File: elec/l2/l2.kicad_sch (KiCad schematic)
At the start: 26 parts, among them J1 Conn_01x06, J2 Conn_01x06, J3 Conn_01x04, U2 DEV-15583, U28 xiao-esp32c3

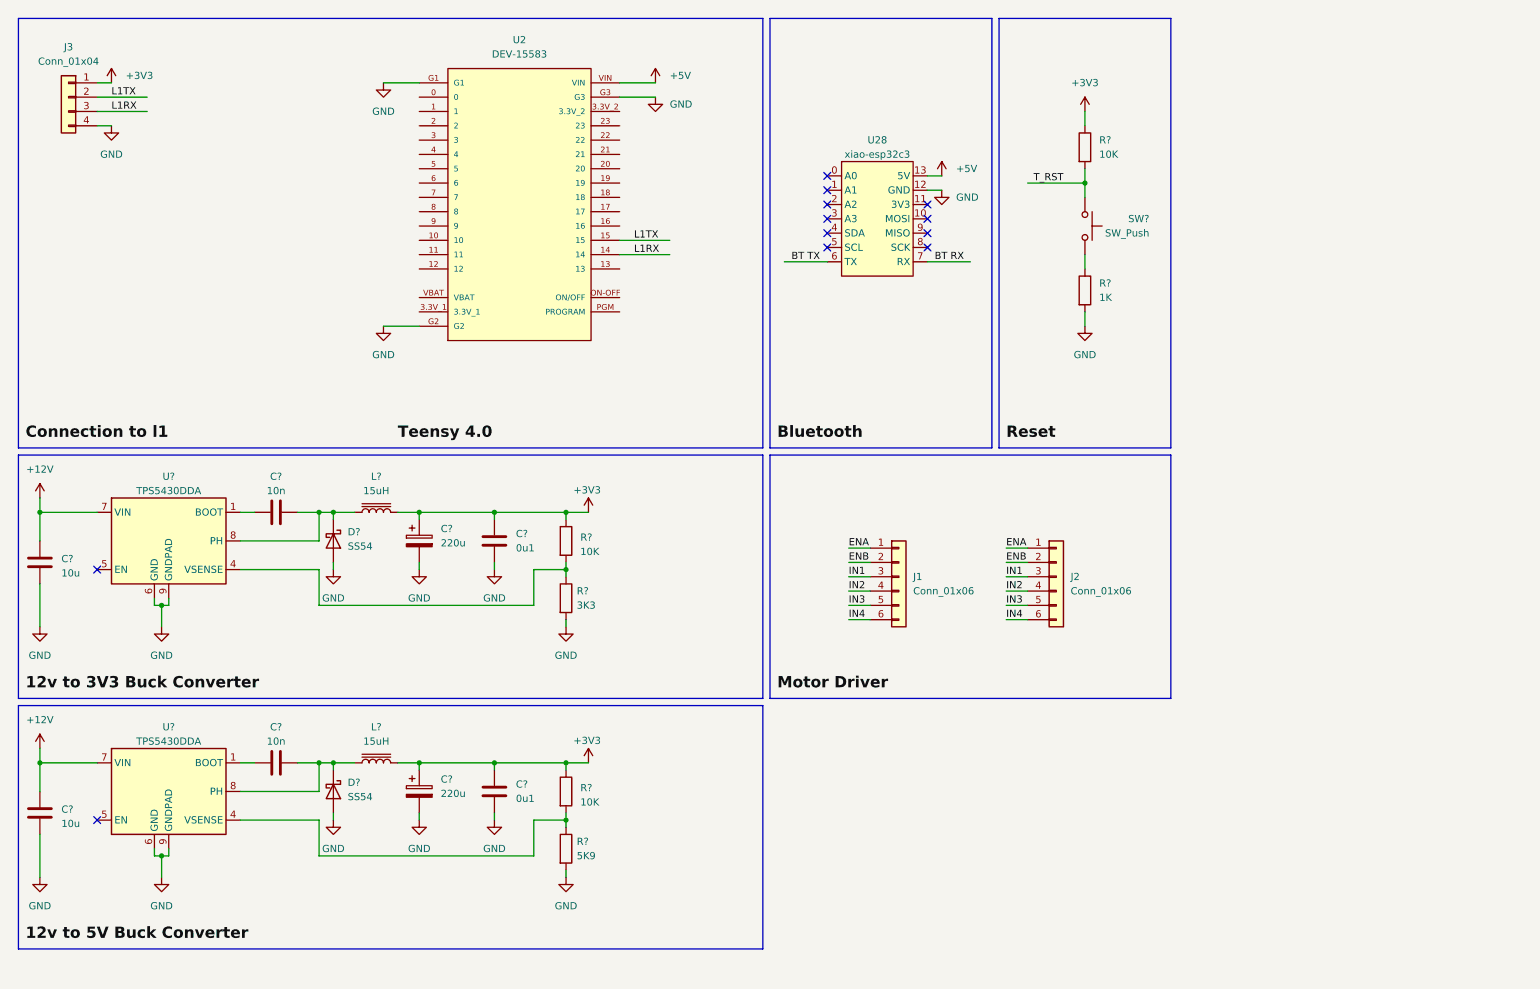
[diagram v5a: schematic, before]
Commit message: producion l1, fucked l2 need to redo, todo: l2,l3
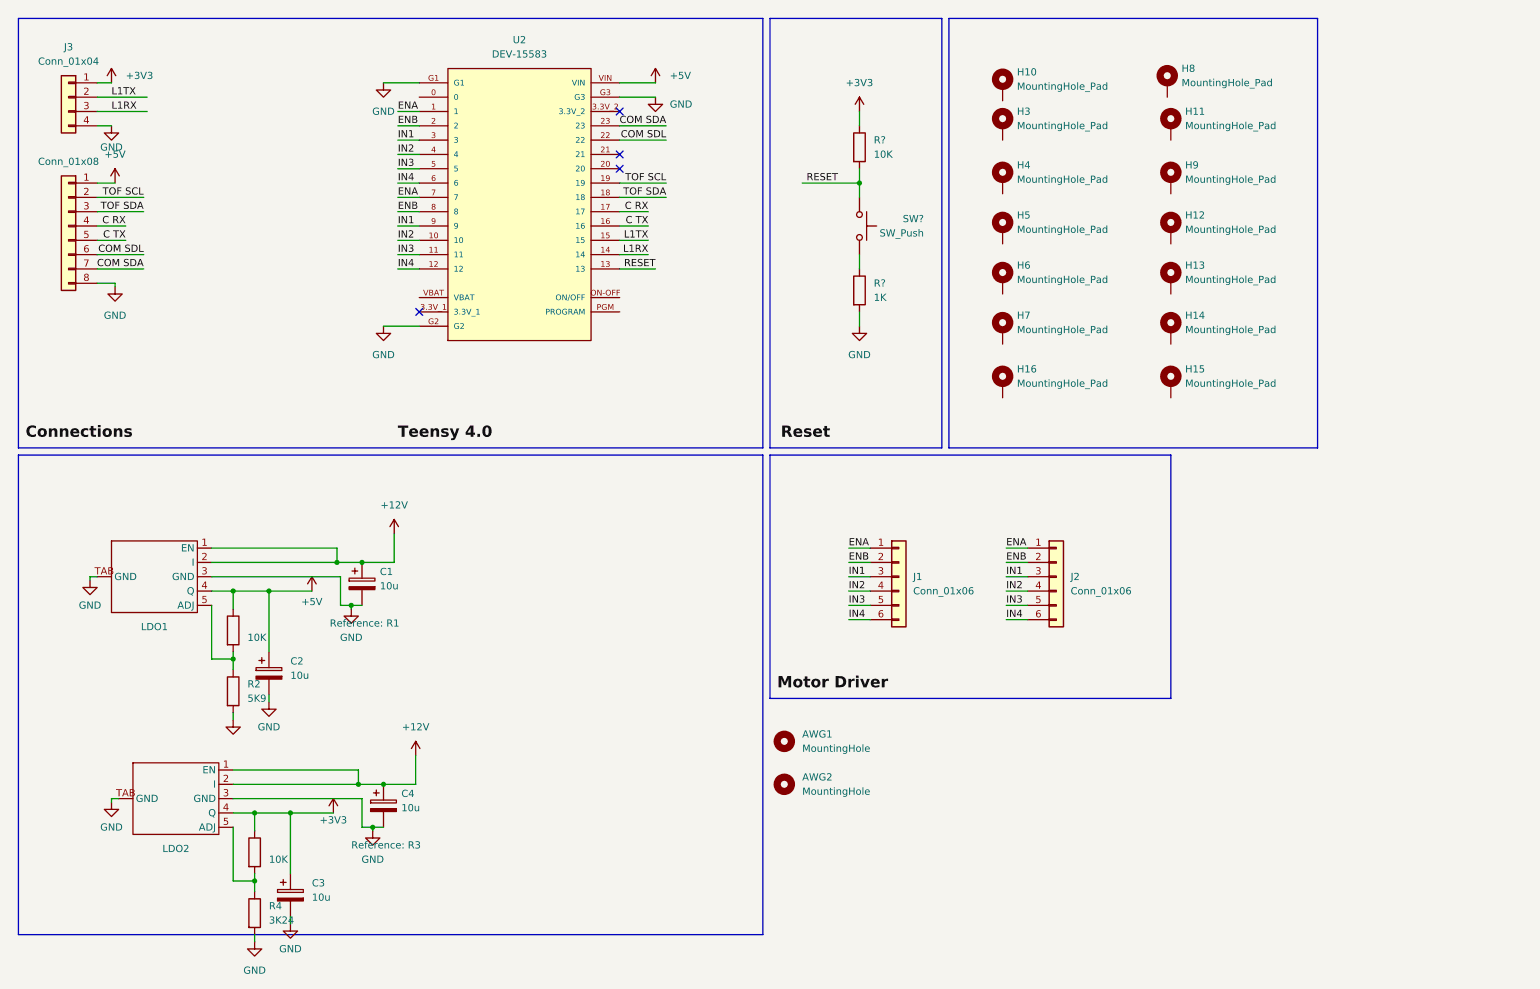
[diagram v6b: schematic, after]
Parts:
- removed C? (x2): 0u1, l2:cap0603, symbol Device:C
- removed C? (x2): 10u, l2:cap0603, symbol Device:C
- removed C? (x2): 220u, l2:EIA-7343-D, symbol Device:C_Polarized
- removed C? (x2): 10n, l2:cap0603, symbol Device:C
- removed D? (x2): SS54, l2:SMA (DO-214AC), symbol Diode:B340
- removed L? (x2): 15uH, l2:0630 One Piece Inductor, symbol Device:L_Iron
- removed R?: 5K9, l2:res0603, symbol Device:R
- removed R?: 3K3, l2:res0603, symbol Device:R
- removed R? (x2): 10K, l2:res0603, symbol Device:R
- removed U28: xiao-esp32c3, footprints:xiao-esp32c3, symbol Seeed_Studio_XIAO_Series:xiao-esp32c3
- removed U? (x2): TPS5430DDA, l2:TI_SO-PowerPAD-8, symbol Regulator_Switching:TPS5430DDA
- added AWG1, AWG2: MountingHole, l2:14 AWG, symbol Mechanical:MountingHole
- added C1, C2, C3, C4: 10u, l2:cap0603, symbol Device:C_Polarized
- added H10, H11, H12, H13, H14, H15, H16, H3, H4, H5, H6, H7, H8, H9: MountingHole_Pad, MountingHole:MountingHole_3.2mm_M3_Pad_Via, symbol Mechanical:MountingHole_Pad
- added J5: Conn_01x08, Connector_PinSocket_2.54mm:PinSocket_1x08_P2.54mm_Vertical, symbol Connector_Generic:Conn_01x08
- added LDO1, LDO2: ~, TLF1963:TLF1963TBATMA1 footprint, symbol hy:TLF1963
- added R1, R3: 10K, l2:res0603, symbol Device:R
- added R2: 5K9, l2:res0603, symbol Device:R
- added R4: 3K24, l2:res0603, symbol Device:R
- J1, J2: footprint Connector_PinSocket_1.00mm:PinSocket_1x06_P1.00mm_Vertical -> hy:L298N
- U2: footprint DEV-15583:MODULE_DEV-15583 -> SparkFun DEV-155:MODULE_DEV-15583
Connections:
- net T_RST is gone; now on net RESET: R?.2, SW?.2
- net +12V: now also C1.1, C4.1, LDO1.1 (EN), LDO1.2 (I), LDO2.1 (EN), LDO2.2 (I)
- net +3V3: now also C3.1, LDO2.4 (Q), R3.1
- net +5V: now also C2.1, J5.1 (Pin_1), LDO1.4 (Q), R1.1
- net ENA: now also U2.1, U2.7
- net ENB: now also U2.2, U2.8
- net GND: now also C1.2, C2.2, C3.2, C4.2, J5.8 (Pin_8), LDO1.3 (GND), LDO1.TAB (GND), LDO2.3 (GND), LDO2.TAB (GND), R2.2, R4.2
- net IN1: now also U2.3, U2.9
- net IN2: now also U2.10, U2.4
- net IN3: now also U2.11, U2.5
- net IN4: now also U2.12, U2.6
- net RESET: now reaches U2.13
- net C TX: now reaches U2.16
- net C TX: now also J5.5 (Pin_5)
- net C RX: now reaches U2.17
- net C RX: now also J5.4 (Pin_4)
- net TOF SDA: now reaches U2.18
- net TOF SDA: now also J5.3 (Pin_3)
- net TOF SCL: now reaches U2.19
- net TOF SCL: now also J5.2 (Pin_2)
- net COM SDL: now reaches U2.22
- net COM SDL: now also J5.6 (Pin_6)
- net COM SDA: now reaches U2.23
- net COM SDA: now also J5.7 (Pin_7)
- new net: LDO2.5 (ADJ), R3.2, R4.1
- new net: LDO1.5 (ADJ), R1.2, R2.1
- no-connect marks 12 -> 4
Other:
- moved on the sheet: R?, SW?

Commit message: 2024-02-28 production
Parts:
- removed AWG1, AWG2: MountingHole, l2:14 AWG, symbol Mechanical:MountingHole
- removed C1, C3, C4: 10u, l2:cap0603, symbol Device:C_Polarized
- removed J1, J2: Conn_01x06, hy:L298N, symbol Connector_Generic:Conn_01x06
- removed LDO1, LDO2: ~, TLF1963:TLF1963TBATMA1 footprint, symbol hy:TLF1963
- added C1: 10n, l2:cap0603, symbol Device:C
- added C3, C6: C, l2:cap0603, symbol Device:C
- added C4: 10u, l2:cap0603, symbol Device:C
- added C5: 220u, l2:EIA-7343-D, symbol Device:C_Polarized
- added D1, D2: B340, hy:DIOM5025X220N, symbol Diode:B340
- added H1, H2: MountingHole_Pad, MountingHole:MountingHole_3.2mm_M3_Pad_Via, symbol Mechanical:MountingHole_Pad
- added J1, J2: Conn_01x13, hy:L298N, symbol Connector_Generic:Conn_01x13
- added L1, L2: 15uH, l2:0630 One Piece Inductor, symbol Device:L_Iron
- added U? (x2): TPS5430DDA, l2:TI_SO-PowerPAD-8, symbol Regulator_Switching:TPS5430DDA
- added batawg1, batawg2: +12V, l2:14 AWG, symbol Connector:TestPoint
- C2: value 10u -> 220u; footprint l2:cap0603 -> l2:EIA-7343-D
- J3: footprint Connector_PinSocket_1.27mm:PinSocket_1x04_P1.27mm_Vertical -> Connector_PinHeader_2.54mm:PinHeader_1x04_P2.54mm_Vertical
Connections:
- net +12V: now also U2.VBAT, C3.1, C6.1, J1.3 (Pin_3), J2.3 (Pin_3), U?.7 (VIN), U?.7 (VIN), batawg1.1, batawg2.1
- net +3V3: now also C5.1, L2.2
- net +5V: now also J1.5 (Pin_5), J2.5 (Pin_5), L1.2
- net C RX: now also U2.21; no longer U2.17
- net C TX: now also U2.20; no longer U2.16
- net COM SDA: now also U2.16; no longer U2.23
- net COM SDL: now also U2.17; no longer U2.22
- net GND: now also C3.2, C5.2, C6.2, D1.2 (A), D2.2 (A), J1.4 (Pin_4), J2.4 (Pin_4), U?.6 (GND), U?.6 (GND), U?.9 (GNDPAD), U?.9 (GNDPAD)
- net RESET: now also U2.ON-OFF (ON/OFF); no longer U2.13
- net at R3.2, R4.1: now also U?.4 (VSENSE)
- net at R1.2, R2.1: now also U?.4 (VSENSE)
- net 1-ENA: now reaches U2.0
- net 1-ENA: now also J1.6 (Pin_6)
- net ENA renamed 1-IN1
- net 1-IN1: now also J1.7 (Pin_7); no longer U2.7
- net ENB renamed 1-IN2
- net 1-IN2: now also J1.8 (Pin_8); no longer U2.8
- net IN1 renamed 1-IN3
- net 1-IN3: now also J1.9 (Pin_9); no longer U2.9
- net IN2 renamed 1-IN4
- net 1-IN4: now also J1.10 (Pin_10); no longer U2.10
- net IN3 renamed 1-ENB
- net 1-ENB: now also J1.11 (Pin_11); no longer U2.11
- net IN4: no longer names the net of U2.12
- net IN4: no longer U2.6
- new net: C1.2, D1.1 (K), L1.1, U?.8 (PH)
- new net: C4.1, D2.1 (K), L2.1, U?.8 (PH)
- new net: C4.2, U?.1 (BOOT)
- new net: C1.1, U?.1 (BOOT)
- new net 2-ENA: J2.6 (Pin_6), U2.6
- new net 2-ENB: J2.11 (Pin_11), U2.11
- new net 2-IN1: J2.7 (Pin_7), U2.7
- new net 2-IN2: J2.8 (Pin_8), U2.8
- new net 2-IN3: J2.9 (Pin_9), U2.9
- new net 2-IN4: J2.10 (Pin_10), U2.10
- no-connect marks 4 -> 31
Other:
- note added: "Buck Converter (12v to 3V3, 12V to 5V)"
- note added: "Connections"
- note added: "Teensy 4.0"
